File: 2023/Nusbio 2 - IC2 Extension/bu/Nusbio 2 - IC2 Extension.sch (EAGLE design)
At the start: 18 parts

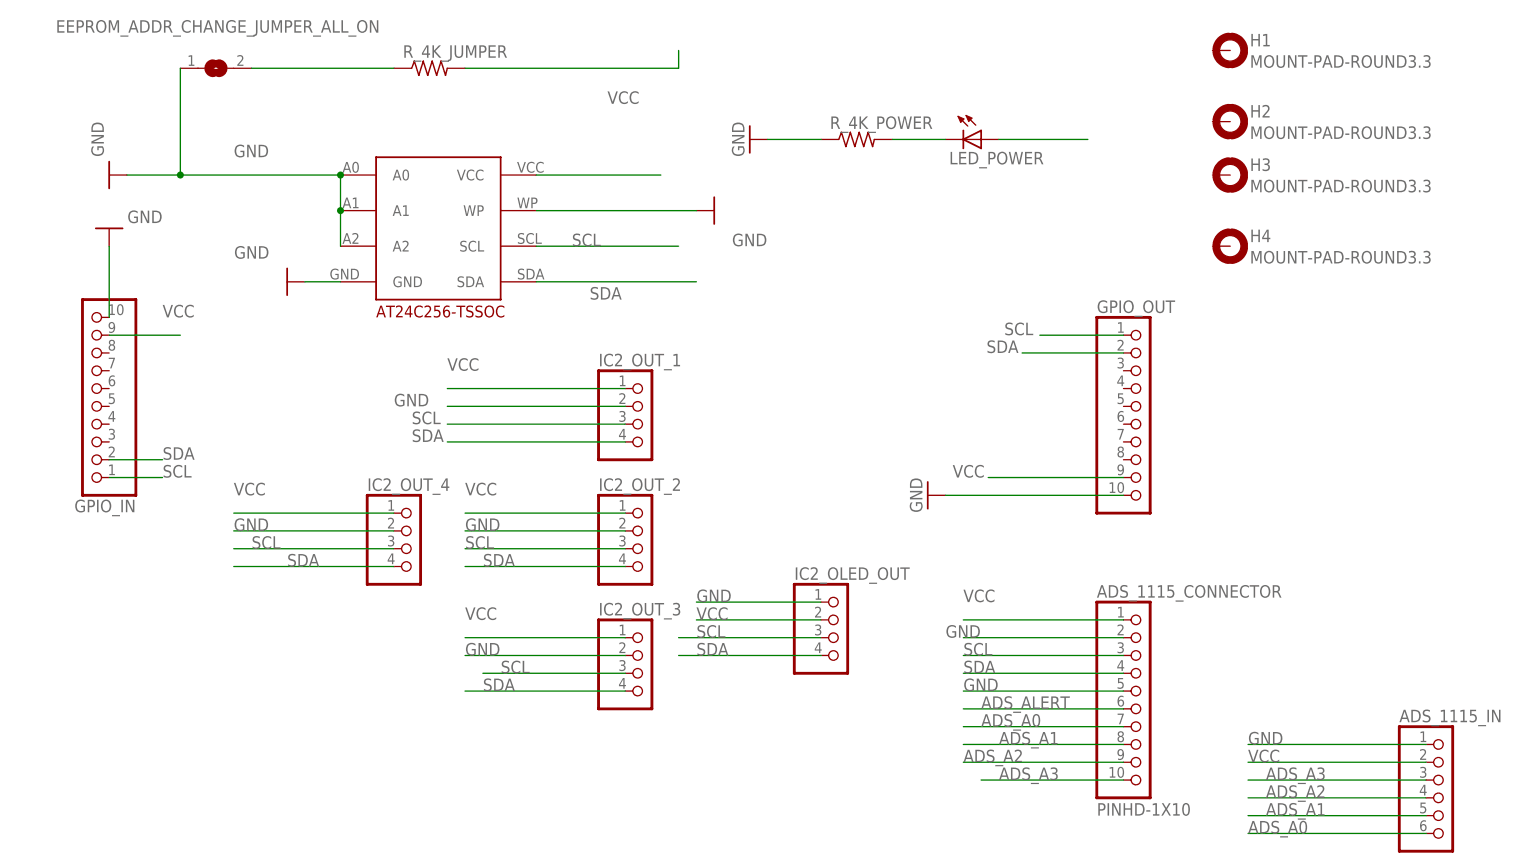
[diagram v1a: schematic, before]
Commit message: Fix Nusbio I2Cextension with right eeprom format
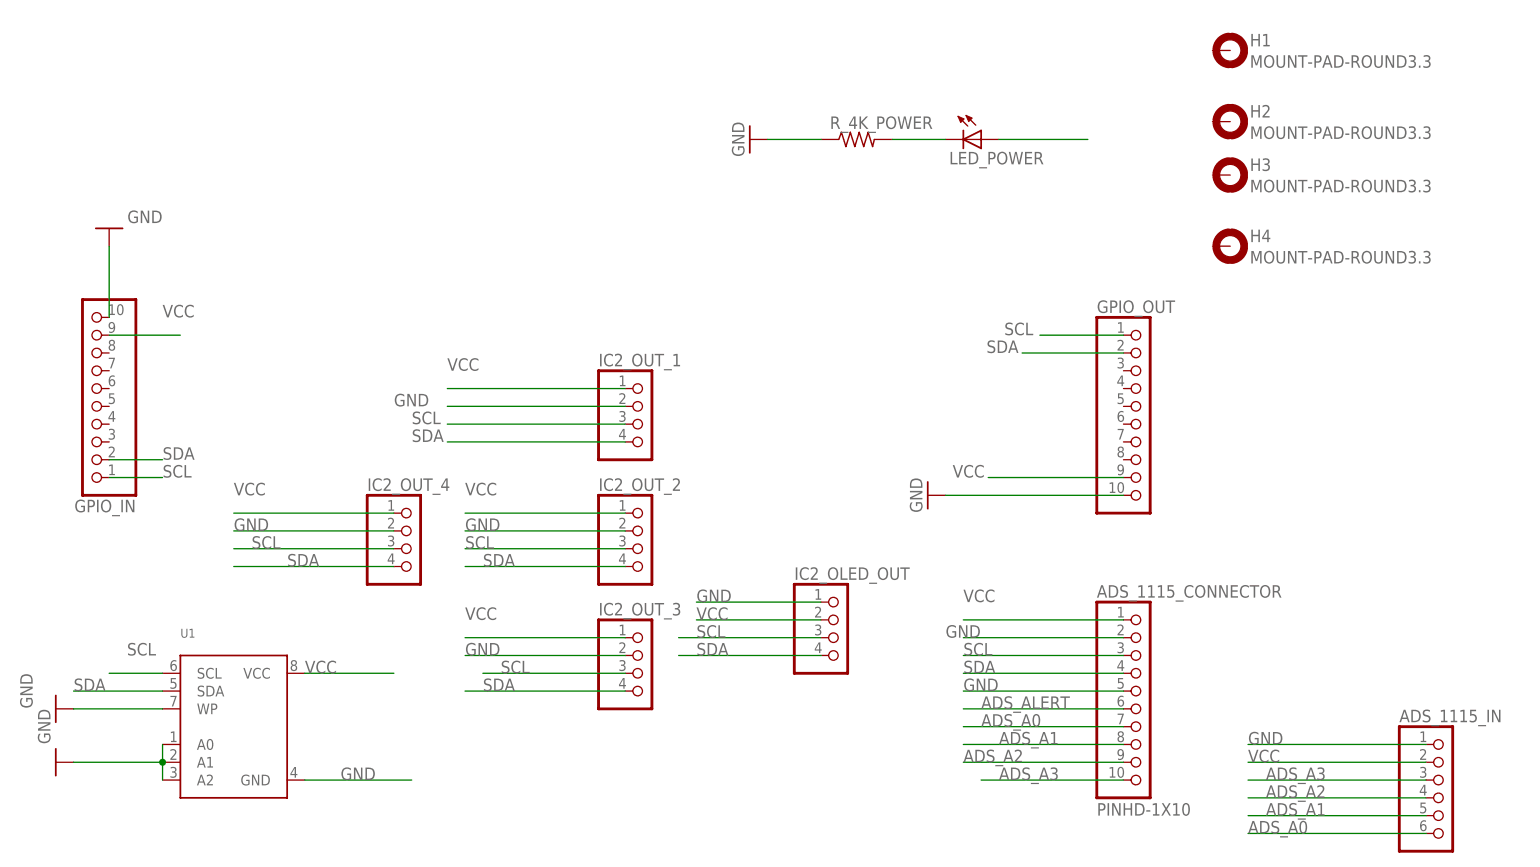
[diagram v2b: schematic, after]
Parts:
- removed EEPROM_ADDR_CHANGE_JUMPER_ALL_ON: (no value), microbuilder:SOLDERJUMPERREFLOW
- removed EEPROM_AT24C256: DECADE-AT24C256-10TI-2.7, DECADE-libraries20151104:DECADE-AT24C256-10TI-2.7
- removed R_4K_JUMPER: (no value), adafruit:R-US_R1206
- added U1: (no value), microbuilder:EEPROM_I2C_SOIC8_GENERIC
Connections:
- removed net N$1: EEPROM_AT24C256.VCC
- removed net N$6: EEPROM_ADDR_CHANGE_JUMPER_ALL_ON.2, R_4K_JUMPER.1
- net GND: now also U1.A0, U1.A1, U1.A2, U1.GND, U1.WP; no longer EEPROM_ADDR_CHANGE_JUMPER_ALL_ON.1, EEPROM_AT24C256.A0, EEPROM_AT24C256.A1, EEPROM_AT24C256.A2, EEPROM_AT24C256.GND, EEPROM_AT24C256.WP
- net SCL: now also U1.SCL; no longer EEPROM_AT24C256.SCL
- net SDA: now also U1.SDA; no longer EEPROM_AT24C256.SDA
- net VCC: now also U1.VCC; no longer R_4K_JUMPER.2
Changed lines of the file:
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@@
 <part name="LED_POWER" library="adafruit" deviceset="LED" device="SMT1206"/>
 <part name="GND4" library="supply1" deviceset="GND" device=""/>
-<part name="EEPROM_AT24C256" library="DECADE-libraries20151104" deviceset="DECADE-AT24C256-10TI-2.7" device=""/>
-<part name="GND2" library="supply1" deviceset="GND" device=""/>
-<part name="EEPROM_ADDR_CHANGE_JUMPER_ALL_ON" library="microbuilder" deviceset="SOLDERJUMPER" device="REFLOW"/>
-<part name="R_4K_JUMPER" library="adafruit" deviceset="R-US_" device="R1206"/>
-<part name="GND5" library="supply1" deviceset="GND" device=""/>
 <part name="IC2_OUT_1" library="pinhead" library_urn="urn:adsk.eagle:library:325" deviceset="PINHD-1X4" device="" package3d_urn="urn:adsk.eagle:package:22407/2"/>
 <part name="IC2_OUT_2" library="pinhead" library_urn="urn:adsk.eagle:library:325" deviceset="PINHD-1X4" device="" package3d_urn="urn:adsk.eagle:package:22407/2"/>
@@
 <part name="ADS_1115_CONNECTOR" library="adafruit" deviceset="PINHD-1X10" device=""/>
 <part name="ADS_1115_IN" library="adafruit" deviceset="PINHD-1X6" device=""/>
-<part name="GND6" library="supply1" deviceset="GND" device=""/>
 <part name="H1" library="holes" library_urn="urn:adsk.eagle:library:237" deviceset="MOUNT-PAD-ROUND" device="3.3" package3d_urn="urn:adsk.eagle:package:14283/1"/>
 <part name="H2" library="holes" library_urn="urn:adsk.eagle:library:237" deviceset="MOUNT-PAD-ROUND" device="3.3" package3d_urn="urn:adsk.eagle:package:14283/1"/>
 <part name="H3" library="holes" library_urn="urn:adsk.eagle:library:237" deviceset="MOUNT-PAD-ROUND" device="3.3" package3d_urn="urn:adsk.eagle:package:14283/1"/>
 <part name="H4" library="holes" library_urn="urn:adsk.eagle:library:237" deviceset="MOUNT-PAD-ROUND" device="3.3" package3d_urn="urn:adsk.eagle:package:14283/1"/>
+<part name="U1" library="microbuilder" deviceset="EEPROM_I2C_SOIC8_GENERIC" device=""/>
+<part name="GND7" library="supply1" deviceset="GND" device=""/>
+<part name="GND8" library="supply1" deviceset="GND" device=""/>
 </parts>
 <sheets>
@@
 <attribute name="VALUE" x="76.2" y="96.52" size="1.778" layer="96" rot="R270"/>
 </instance>
-<instance part="EEPROM_AT24C256" gate="G$1" x="30.48" y="76.2" smashed="yes"/>
-<instance part="GND2" gate="1" x="12.7" y="73.66" smashed="yes" rot="R270">
-<attribute name="VALUE" x="10.16" y="78.74" size="1.778" layer="96" rot="R180"/>
-</instance>
-<instance part="EEPROM_ADDR_CHANGE_JUMPER_ALL_ON" gate="1" x="2.54" y="104.14" smashed="yes">
-<attribute name="NAME" x="-20.32" y="109.22" size="1.778" layer="95"/>
-<attribute name="VALUE" x="0" y="100.33" size="1.778" layer="96"/>
-</instance>
-<instance part="R_4K_JUMPER" gate="G$1" x="33.02" y="104.14" smashed="yes">
-<attribute name="NAME" x="29.21" y="105.6386" size="1.778" layer="95"/>
-<attribute name="VALUE" x="29.21" y="100.838" size="1.778" layer="96"/>
-</instance>
-<instance part="GND5" gate="1" x="-12.7" y="88.9" smashed="yes" rot="R270">
-<attribute name="VALUE" x="-15.24" y="96.52" size="1.778" layer="96" rot="R270"/>
-</instance>
 <instance part="IC2_OUT_1" gate="A" x="63.5" y="53.34" smashed="yes">
 <attribute name="NAME" x="57.15" y="61.595" size="1.778" layer="95"/>
@@
 <attribute name="VALUE" x="171.45" y="-10.16" size="1.778" layer="96"/>
 </instance>
-<instance part="GND6" gate="1" x="73.66" y="83.82" smashed="yes" rot="R90">
-<attribute name="VALUE" x="76.2" y="78.74" size="1.778" layer="96"/>
-</instance>
 <instance part="H1" gate="G$1" x="147.32" y="106.68" smashed="yes">
 <attribute name="NAME" x="150.114" y="107.2642" size="1.778" layer="95"/>
@@
 <attribute name="NAME" x="150.114" y="79.3242" size="1.778" layer="95"/>
 <attribute name="VALUE" x="150.114" y="76.2762" size="1.778" layer="96"/>
+</instance>
+<instance part="U1" gate="G$1" x="5.08" y="10.16" smashed="yes">
+<attribute name="NAME" x="-2.54" y="22.86" size="1.27" layer="95"/>
+<attribute name="VALUE" x="-2.54" y="-2.54" size="1.27" layer="96"/>
+</instance>
+<instance part="GND7" gate="1" x="-20.32" y="12.7" smashed="yes" rot="R270">
+<attribute name="VALUE" x="-25.4" y="17.78" size="1.778" layer="96" rot="R270"/>
+</instance>
+<instance part="GND8" gate="1" x="-20.32" y="5.08" smashed="yes" rot="R270">
+<attribute name="VALUE" x="-22.86" y="12.7" size="1.778" layer="96" rot="R270"/>
 </instance>
 </instances>
@@
 </segment>
 <segment>
-<pinref part="GND2" gate="1" pin="GND"/>
-<pinref part="EEPROM_AT24C256" gate="G$1" pin="GND"/>
-<wire x1="15.24" y1="73.66" x2="20.32" y2="73.66" width="0.1524" layer="91"/>
-</segment>
-<segment>
-<pinref part="EEPROM_AT24C256" gate="G$1" pin="A2"/>
-<pinref part="EEPROM_AT24C256" gate="G$1" pin="A1"/>
-<wire x1="20.32" y1="78.74" x2="20.32" y2="83.82" width="0.1524" layer="91"/>
-<pinref part="EEPROM_AT24C256" gate="G$1" pin="A0"/>
-<wire x1="20.32" y1="88.9" x2="20.32" y2="83.82" width="0.1524" layer="91"/>
-<junction x="20.32" y="83.82"/>
-<wire x1="20.32" y1="88.9" x2="-2.54" y2="88.9" width="0.1524" layer="91"/>
-<junction x="20.32" y="88.9"/>
-<label x="5.08" y="91.44" size="1.778" layer="95"/>
-<pinref part="GND5" gate="1" pin="GND"/>
-<pinref part="EEPROM_ADDR_CHANGE_JUMPER_ALL_ON" gate="1" pin="1"/>
-<wire x1="-2.54" y1="88.9" x2="-10.16" y2="88.9" width="0.1524" layer="91"/>
-<wire x1="-2.54" y1="104.14" x2="-2.54" y2="88.9" width="0.1524" layer="91"/>
-<junction x="-2.54" y="88.9"/>
-</segment>
-<segment>
 <pinref part="IC2_OUT_1" gate="A" pin="2"/>
 <wire x1="60.96" y1="55.88" x2="35.56" y2="55.88" width="0.1524" layer="91"/>
@@
 </segment>
 <segment>
-<pinref part="EEPROM_AT24C256" gate="G$1" pin="WP"/>
-<pinref part="GND6" gate="1" pin="GND"/>
-<wire x1="48.26" y1="83.82" x2="71.12" y2="83.82" width="0.1524" layer="91"/>
+<pinref part="U1" gate="G$1" pin="GND"/>
+<wire x1="15.24" y1="2.54" x2="30.48" y2="2.54" width="0.1524" layer="91"/>
+<label x="20.32" y="2.54" size="1.778" layer="95"/>
+</segment>
+<segment>
+<pinref part="U1" gate="G$1" pin="WP"/>
+<pinref part="GND7" gate="1" pin="GND"/>
+<wire x1="-5.08" y1="12.7" x2="-17.78" y2="12.7" width="0.1524" layer="91"/>
+</segment>
+<segment>
+<pinref part="U1" gate="G$1" pin="A0"/>
+<pinref part="U1" gate="G$1" pin="A1"/>
+<wire x1="-5.08" y1="7.62" x2="-5.08" y2="5.08" width="0.1524" layer="91"/>
+<pinref part="U1" gate="G$1" pin="A2"/>
+<wire x1="-5.08" y1="2.54" x2="-5.08" y2="5.08" width="0.1524" layer="91"/>
+<junction x="-5.08" y="5.08"/>
+<pinref part="GND8" gate="1" pin="GND"/>
+<wire x1="-5.08" y1="5.08" x2="-17.78" y2="5.08" width="0.1524" layer="91"/>
 </segment>
 </net>
@@
 </segment>
 <segment>
-<pinref part="R_4K_JUMPER" gate="G$1" pin="2"/>
-<wire x1="38.1" y1="104.14" x2="68.58" y2="104.14" width="0.1524" layer="91"/>
-<wire x1="68.58" y1="104.14" x2="68.58" y2="106.68" width="0.1524" layer="91"/>
-<label x="58.42" y="99.06" size="1.778" layer="95"/>
-</segment>
-<segment>
 <pinref part="IC2_OLED_OUT" gate="A" pin="2"/>
 <wire x1="88.9" y1="25.4" x2="71.12" y2="25.4" width="0.1524" layer="91"/>
 <label x="71.12" y="25.4" size="1.778" layer="95"/>
 </segment>
+<segment>
+<pinref part="U1" gate="G$1" pin="VCC"/>
+<wire x1="15.24" y1="17.78" x2="27.94" y2="17.78" width="0.1524" layer="91"/>
+<label x="15.24" y="17.78" size="1.778" layer="95"/>
+</segment>
 </net>
 <net name="N$2" class="0">
@@
 </segment>
 <segment>
-<pinref part="EEPROM_AT24C256" gate="G$1" pin="SCL"/>
-<wire x1="48.26" y1="78.74" x2="68.58" y2="78.74" width="0.1524" layer="91"/>
-<label x="53.34" y="78.74" size="1.778" layer="95"/>
-</segment>
-<segment>
 <pinref part="IC2_OUT_1" gate="A" pin="3"/>
 <wire x1="60.96" y1="53.34" x2="35.56" y2="53.34" width="0.1524" layer="91"/>
@@
 <label x="109.22" y="20.32" size="1.778" layer="95"/>
 </segment>
+<segment>
+<pinref part="U1" gate="G$1" pin="SCL"/>
+<wire x1="-5.08" y1="17.78" x2="-12.7" y2="17.78" width="0.1524" layer="91"/>
+<label x="-10.16" y="20.32" size="1.778" layer="95"/>
+</segment>
 </net>
 <net name="SDA" class="0">
@@
 </segment>
 <segment>
-<pinref part="EEPROM_AT24C256" gate="G$1" pin="SDA"/>
-<wire x1="48.26" y1="73.66" x2="71.12" y2="73.66" width="0.1524" layer="91"/>
-<label x="55.88" y="71.12" size="1.778" layer="95"/>
-</segment>
-<segment>
 <pinref part="IC2_OUT_1" gate="A" pin="4"/>
 <wire x1="60.96" y1="50.8" x2="35.56" y2="50.8" width="0.1524" layer="91"/>
@@
 <label x="109.22" y="17.78" size="1.778" layer="95"/>
 </segment>
-</net>
-<net name="N$1" class="0">
-<segment>
-<pinref part="EEPROM_AT24C256" gate="G$1" pin="VCC"/>
-<wire x1="48.26" y1="88.9" x2="66.04" y2="88.9" width="0.1524" layer="91"/>
-</segment>
-</net>
-<net name="N$6" class="0">
-<segment>
-<pinref part="R_4K_JUMPER" gate="G$1" pin="1"/>
-<pinref part="EEPROM_ADDR_CHANGE_JUMPER_ALL_ON" gate="1" pin="2"/>
-<wire x1="27.94" y1="104.14" x2="7.62" y2="104.14" width="0.1524" layer="91"/>
-</segment>
-</net>
+<segment>
+<pinref part="U1" gate="G$1" pin="SDA"/>
+<wire x1="-5.08" y1="15.24" x2="-17.78" y2="15.24" width="0.1524" layer="91"/>
+<label x="-17.78" y="15.24" size="1.778" layer="95"/>
+</segment>
+</net>
